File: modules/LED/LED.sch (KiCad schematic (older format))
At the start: 50 parts, among them J1 2, J10 11, J11 12, J12 13, J13 A0, J14 A1, J15 A2, J16 A3, J17 A4, J18 A5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

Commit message: LED rework
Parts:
- removed Q? (x4): IRLML2060, Package_TO_SOT_SMD:SOT-23, symbol Transistor_FET:IRLML2060
- removed R?: 10k, symbol Device:R
- removed U1: 4511, Package_SO:SOIC-16_3.9x9.9mm_P1.27mm, symbol 4xxx_IEEE:4511
- removed U?: 74HC238, symbol 74xx_IEEE:74HC238
- added Q1, Q2, Q3, Q4: IRLML6402, Package_TO_SOT_SMD:SOT-23, symbol Transistor_FET:IRLML6402
- added R14: R, Resistor_SMD:R_0805_2012Metric_Pad1.15x1.40mm_HandSolder, symbol Device:R
- added U1: 74LS247, Package_SO:SOIC-16_3.9x9.9mm_P1.27mm, symbol 74xx:74LS247
- added U2: 74LS139, Package_SO:SOIC-16_3.9x9.9mm_P1.27mm, symbol 74xx_IEEE:74LS139
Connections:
- wire segments 123 -> 107
- no-connect marks 11 -> 17
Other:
- note added: "CA"
- note removed: "CC"
- moved on the sheet: C1, D1, D2, D4, D5, R12

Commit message: Fix LED pcb
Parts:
- removed R14: R, Resistor_SMD:R_0805_2012Metric_Pad1.15x1.40mm_HandSolder, symbol Device:R
- renumbered L1 to HL1
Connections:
- net labels added: D0, D1, D2, D3, Line0
- wire segments 107 -> 108
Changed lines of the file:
@@
 $EndComp
 $Comp
-L CommonLibrary:7seg-4dig-0.4inch L1
+L CommonLibrary:7seg-4dig-0.4inch HL1
 U 1 1 5D7B3B0A
 P 4150 4050
-F 0 "L1" H 4150 4215 50  0000 C CNN
+F 0 "HL1" H 4150 4215 50  0000 C CNN
 F 1 "7seg-4dig-0.4inch" H 4150 4124 50  0000 C CNN
 F 2 "CommonLibrary:7seg-4dig-0.4inch" H 4175 4675 50  0001 C CNN
@@
 U 1 1 5D7C402B
 P 4950 3050
-F 0 "R11" V 4900 2900 50  0000 C CNN
+F 0 "R11" V 4900 2875 50  0000 C CNN
 F 1 "100" V 4950 3050 50  0000 C CNN
 F 2 "Resistor_SMD:R_0805_2012Metric_Pad1.15x1.40mm_HandSolder" V 4880 3050 50  0001 C CNN
@@
 U 1 1 5D7C4561
 P 4950 2900
-F 0 "R10" V 4900 2750 50  0000 C CNN
+F 0 "R10" V 4900 2725 50  0000 C CNN
 F 1 "100" V 4950 2900 50  0000 C CNN
 F 2 "Resistor_SMD:R_0805_2012Metric_Pad1.15x1.40mm_HandSolder" V 4880 2900 50  0001 C CNN
@@
 U 1 1 5D7C4753
 P 4950 2700
-F 0 "R9" V 4900 2550 50  0000 C CNN
+F 0 "R9" V 4900 2525 50  0000 C CNN
 F 1 "100" V 4950 2700 50  0000 C CNN
 F 2 "Resistor_SMD:R_0805_2012Metric_Pad1.15x1.40mm_HandSolder" V 4880 2700 50  0001 C CNN
@@
 U 1 1 5D7C4A05
 P 4950 2550
-F 0 "R8" V 4900 2400 50  0000 C CNN
+F 0 "R8" V 4900 2375 50  0000 C CNN
 F 1 "100" V 4950 2550 50  0000 C CNN
 F 2 "Resistor_SMD:R_0805_2012Metric_Pad1.15x1.40mm_HandSolder" V 4880 2550 50  0001 C CNN
@@
 U 1 1 5D806B1E
 P 5900 1875
-F 0 "R12" V 5825 1925 50  0000 L CNN
+F 0 "R12" V 5800 1825 50  0000 L CNN
 F 1 "10k" V 5900 1825 50  0000 L CNN
 F 2 "Resistor_SMD:R_0805_2012Metric_Pad1.15x1.40mm_HandSolder" V 5830 1875 50  0001 C CNN
@@
 U 1 1 5D82C9F4
 P 1825 4750
-F 0 "R13" H 1895 4796 50  0000 L CNN
-F 1 "10k" H 1895 4705 50  0000 L CNN
+F 0 "R13" V 1725 4675 50  0000 L CNN
+F 1 "10k" V 1825 4675 50  0000 L CNN
 F 2 "Resistor_SMD:R_0805_2012Metric_Pad1.15x1.40mm_HandSolder" V 1755 4750 50  0001 C CNN
 F 3 "~" H 1825 4750 50  0001 C CNN
@@
 U 1 1 5D7D571B
 P 6525 4700
-F 0 "C1" H 6525 4825 50  0000 L CNN
-F 1 "0.1uF" H 6525 4525 50  0000 L CNN
+F 0 "C1" H 6550 4825 50  0000 L CNN
+F 1 "0.1uF" H 6550 4550 50  0000 L CNN
 F 2 "Capacitor_SMD:C_0805_2012Metric_Pad1.15x1.40mm_HandSolder" H 6563 4550 50  0001 C CNN
 F 3 "~" H 6525 4700 50  0001 C CNN
@@
 U 2 1 5D9F2012
 P 3725 2800
-F 0 "U2" H 3725 3416 50  0000 C CNN
-F 1 "74LS139" H 3725 3325 50  0000 C CNN
+F 0 "U2" H 3525 3250 50  0000 C CNN
+F 1 "74LS139" H 3925 3250 50  0000 C CNN
 F 2 "Package_SO:SOIC-16_3.9x9.9mm_P1.27mm" H 3725 2800 50  0001 C CNN
 F 3 "" H 3725 2800 50  0001 C CNN
@@
 	2150 4450 1900 4450
 NoConn ~ 1200 2500
-$Comp
-L Device:R R14
-U 1 1 5DA2086C
-P 2150 5100
-F 0 "R14" H 2220 5146 50  0000 L CNN
-F 1 "R" H 2220 5055 50  0000 L CNN
-F 2 "Resistor_SMD:R_0805_2012Metric_Pad1.15x1.40mm_HandSolder" V 2080 5100 50  0001 C CNN
-F 3 "~" H 2150 5100 50  0001 C CNN
-	1    2150 5100
-	1    0    0    -1
-$EndComp
-$Comp
-L power:GND #PWR02
-U 1 1 5DA20E1A
-P 2150 5250
-F 0 "#PWR02" H 2150 5000 50  0001 C CNN
-F 1 "GND" H 2155 5077 50  0000 C CNN
-F 2 "" H 2150 5250 50  0001 C CNN
-F 3 "" H 2150 5250 50  0001 C CNN
-	1    2150 5250
-	1    0    0    -1
-$EndComp
 $Comp
 L power:GND #PWR06
@@
 NoConn ~ 3450 1775
 NoConn ~ 3450 1925
+Text Label 1425 2800 0    50   ~ 0
+D0
+Text Label 1425 2950 0    50   ~ 0
+D1
+Text Label 1425 3100 0    50   ~ 0
+D2
+Text Label 1425 3250 0    50   ~ 0
+D3
+Text Label 1425 3400 0    50   ~ 0
+Line0
+Wire Wire Line
+	2150 4950 2150 4750
+Connection ~ 2150 4750
 $EndSCHEMATC

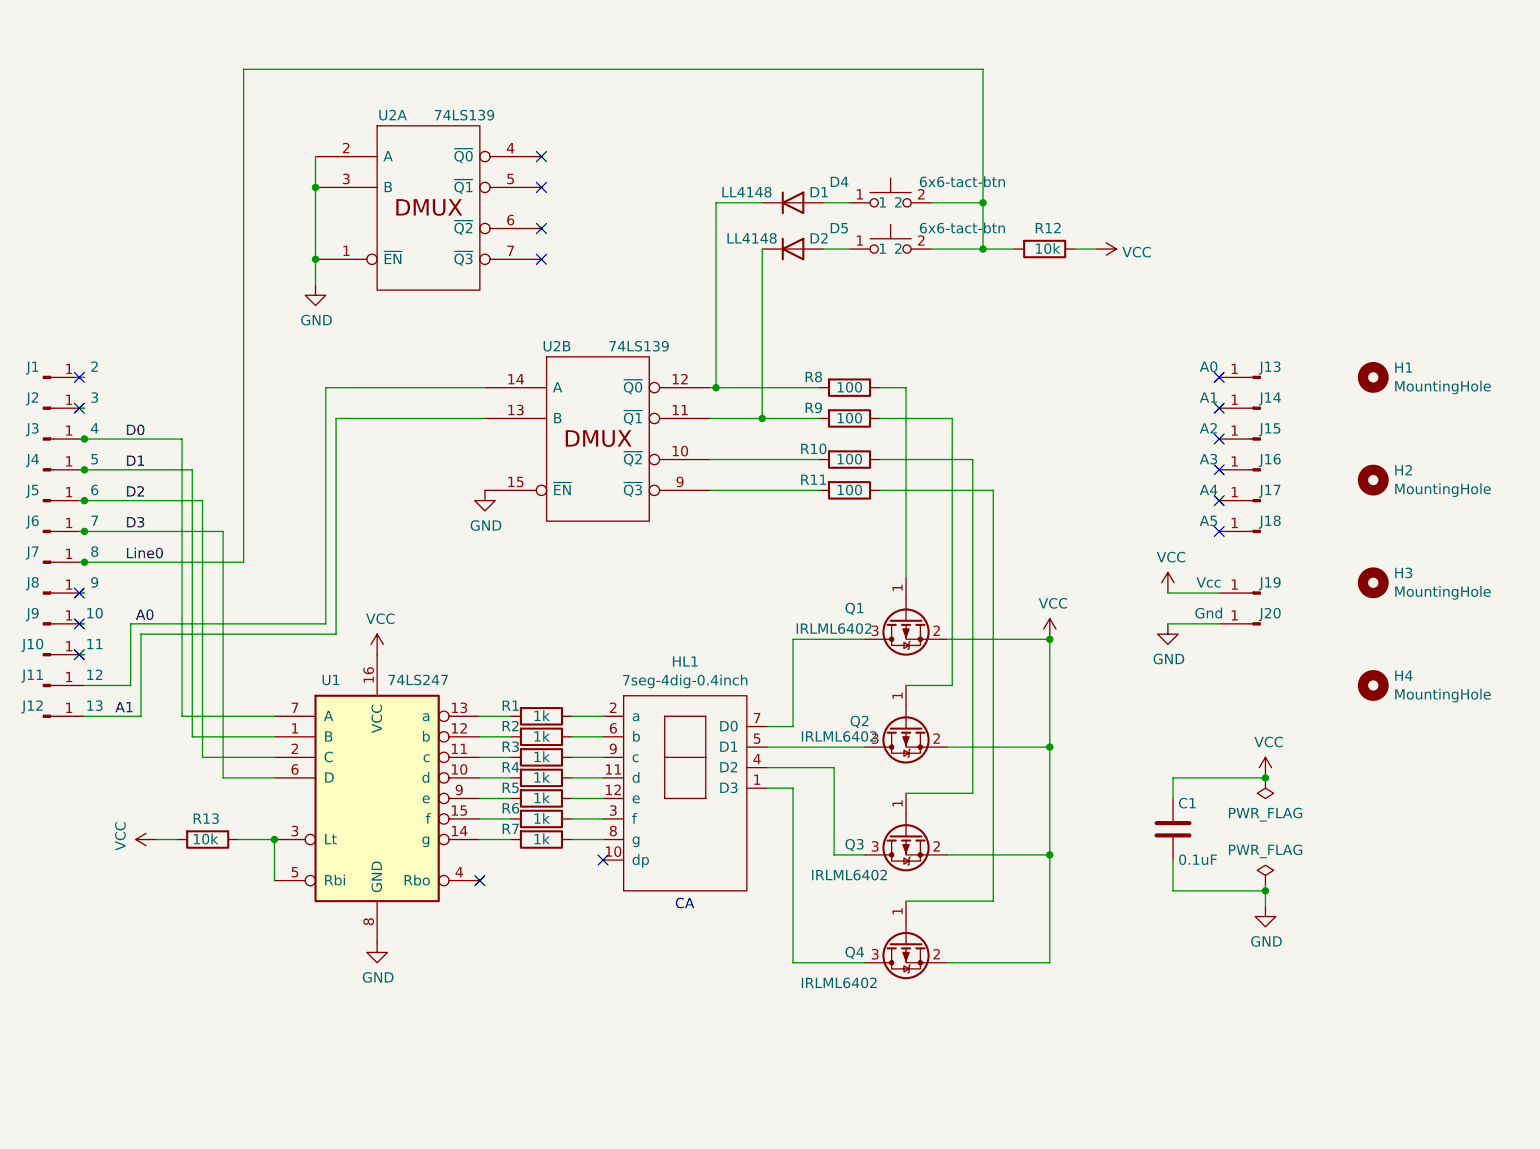
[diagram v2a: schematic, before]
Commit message: LED v2 Pins changed
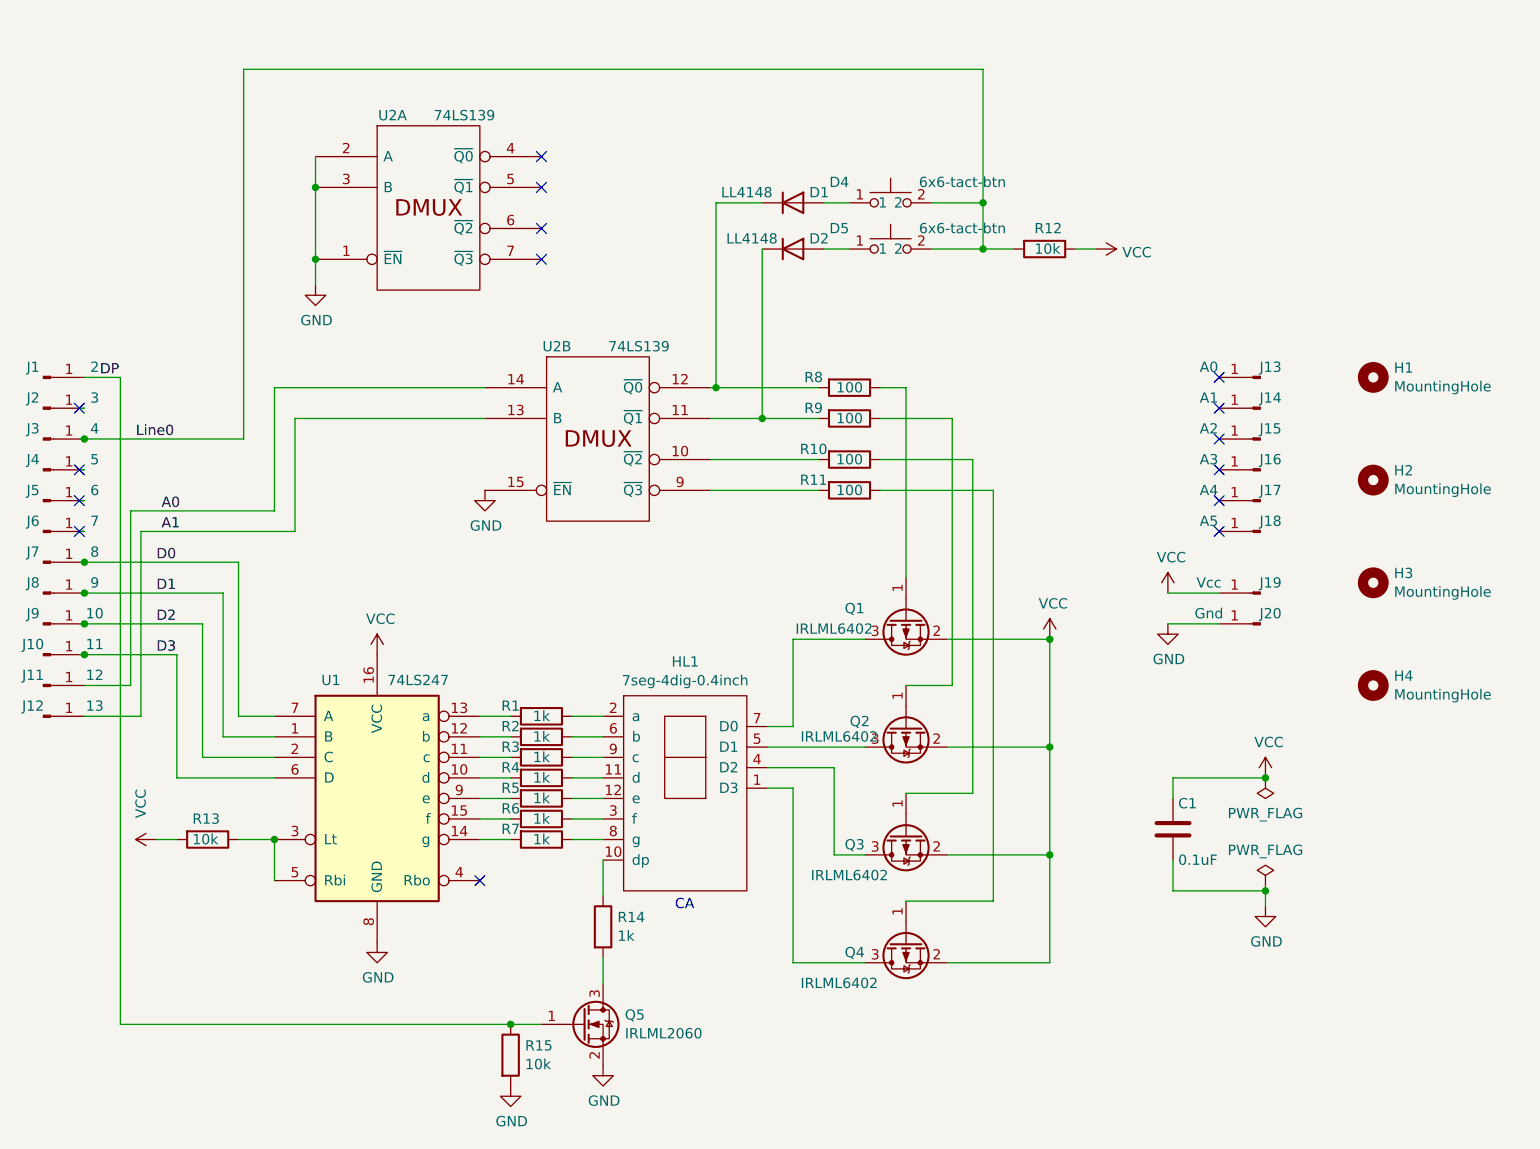
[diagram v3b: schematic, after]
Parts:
- added Q5: IRLML2060, Package_TO_SOT_SMD:SOT-23, symbol Transistor_FET:IRLML2060
- added R14: 1k, Resistor_SMD:R_0805_2012Metric_Pad1.15x1.40mm_HandSolder, symbol Device:R
- added R15: 10k, Resistor_SMD:R_0805_2012Metric_Pad1.15x1.40mm_HandSolder, symbol Device:R
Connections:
- net labels added: DP
- wire segments 108 -> 113
- no-connect marks 17 -> 15
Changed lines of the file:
@@
 P 1575 4750
 F 0 "#PWR0104" H 1575 4600 50  0001 C CNN
-F 1 "VCC" H 1592 4923 50  0000 C CNN
+F 1 "VCC" H 1750 4825 50  0000 C CNN
 F 2 "" H 1575 4750 50  0001 C CNN
 F 3 "" H 1575 4750 50  0001 C CNN
@@
 	1200 2650 1225 2650
 Wire Wire Line
-	1200 2500 1225 2500
-Wire Wire Line
 	1200 2950 1225 2950
 Wire Wire Line
-	1750 2950 1750 4250
-Connection ~ 1225 2950
-Wire Wire Line
-	1225 2950 1750 2950
-Wire Wire Line
 	1200 3100 1225 3100
 Wire Wire Line
-	1800 3100 1800 4350
-Connection ~ 1225 3100
-Wire Wire Line
-	1225 3100 1800 3100
-Wire Wire Line
-	1900 3250 1900 4450
-Wire Wire Line
-	1200 3250 1225 3250
-Connection ~ 1225 3250
-Wire Wire Line
-	1225 3250 1900 3250
-Wire Wire Line
-	1200 2800 1225 2800
-Wire Wire Line
-	1700 2800 1700 4150
-Connection ~ 1225 2800
-Wire Wire Line
-	1225 2800 1700 2800
-Wire Wire Line
-	2000 1000 2000 3400
-Wire Wire Line
-	1200 3400 1225 3400
-Connection ~ 1225 3400
-Wire Wire Line
-	1225 3400 2000 3400
+	2000 1000 2000 2800
 NoConn ~ 1200 2650
 $Comp
@@
 Wire Wire Line
 	1575 4750 1675 4750
-Wire Wire Line
-	1200 3550 1225 3550
-Wire Wire Line
-	1200 3700 1225 3700
-Wire Wire Line
-	1200 3850 1225 3850
 NoConn ~ 6750 3250
 NoConn ~ 6750 2500
@@
 NoConn ~ 6750 2950
 NoConn ~ 6750 3100
-NoConn ~ 3750 4850
 $Comp
 L Mechanical:MountingHole H4
@@
 $EndComp
 Wire Wire Line
-	1450 3700 2400 3700
-Wire Wire Line
-	1450 3700 1450 4000
-Wire Wire Line
-	1500 4150 1500 3750
-Wire Wire Line
-	1500 3750 2450 3750
-Wire Wire Line
 	1225 4150 1500 4150
 Wire Wire Line
 	1225 4000 1450 4000
-NoConn ~ 1200 3700
-NoConn ~ 1200 3850
 $Comp
 L Diode:LL4148 D1
@@
 	1    0    0    -1
 $EndComp
-NoConn ~ 1200 3550
-Text Label 1475 3700 0    50   ~ 0
+Text Label 1600 3150 0    50   ~ 0
 A0
-Text Label 1375 4150 0    50   ~ 0
+Text Label 1600 3250 0    50   ~ 0
 A1
 Text Notes 4100 5100 0    50   ~ 0
@@
 	1975 4750 2150 4750
 Wire Wire Line
-	2150 4150 1700 4150
-Wire Wire Line
-	2150 4250 1750 4250
+	2150 4150 1975 4150
+Wire Wire Line
+	2150 4250 1900 4250
 Wire Wire Line
 	2150 4350 1800 4350
-Wire Wire Line
-	2150 4450 1900 4450
-NoConn ~ 1200 2500
 $Comp
 L power:GND #PWR06
@@
 	1    0    0    -1
 $EndComp
-Wire Wire Line
-	2400 2550 3175 2550
-Wire Wire Line
-	2400 2550 2400 3700
-Wire Wire Line
-	2450 2700 3175 2700
-Wire Wire Line
-	2450 2700 2450 3750
 $Comp
 L Transistor_FET:IRLML6402 Q1
@@
 NoConn ~ 3450 1775
 NoConn ~ 3450 1925
-Text Label 1425 2800 0    50   ~ 0
+Text Label 1575 3400 0    50   ~ 0
 D0
-Text Label 1425 2950 0    50   ~ 0
+Text Label 1575 3550 0    50   ~ 0
 D1
-Text Label 1425 3100 0    50   ~ 0
+Text Label 1575 3700 0    50   ~ 0
 D2
-Text Label 1425 3250 0    50   ~ 0
+Text Label 1575 3850 0    50   ~ 0
 D3
-Text Label 1425 3400 0    50   ~ 0
+Text Label 1475 2800 0    50   ~ 0
 Line0
 Wire Wire Line
 	2150 4950 2150 4750
 Connection ~ 2150 4750
+Wire Wire Line
+	1200 3400 1225 3400
+Connection ~ 1225 3400
+Wire Wire Line
+	1200 3250 1225 3250
+Wire Wire Line
+	1200 3550 1225 3550
+Connection ~ 1225 3550
+Wire Wire Line
+	1200 3700 1225 3700
+Wire Wire Line
+	1800 3700 1800 4350
+Connection ~ 1225 3700
+Wire Wire Line
+	1225 3700 1800 3700
+Wire Wire Line
+	1200 3850 1225 3850
+Connection ~ 1225 3850
+Wire Wire Line
+	1225 3850 1675 3850
+Wire Wire Line
+	1975 3400 1975 4150
+Wire Wire Line
+	1225 3400 1975 3400
+Wire Wire Line
+	1675 3850 1675 4450
+Wire Wire Line
+	1675 4450 2150 4450
+Wire Wire Line
+	1900 3550 1900 4250
+Wire Wire Line
+	1225 3550 1900 3550
+Wire Wire Line
+	1200 2800 1225 2800
+Connection ~ 1225 2800
+Wire Wire Line
+	1225 2800 2000 2800
+Wire Wire Line
+	1500 3250 2250 3250
+Wire Wire Line
+	2250 3250 2250 2700
+Wire Wire Line
+	1500 3250 1500 4150
+Wire Wire Line
+	2250 2700 3175 2700
+Wire Wire Line
+	1450 3150 2150 3150
+Wire Wire Line
+	2150 3150 2150 2550
+Wire Wire Line
+	1450 3150 1450 4000
+Wire Wire Line
+	2150 2550 3175 2550
+NoConn ~ 1200 2950
+NoConn ~ 1200 3100
+NoConn ~ 1200 3250
+$Comp
+L Transistor_FET:IRLML2060 Q5
+U 1 1 5E927114
+P 3650 5650
+F 0 "Q5" H 3856 5696 50  0000 L CNN
+F 1 "IRLML2060" H 3856 5605 50  0000 L CNN
+F 2 "Package_TO_SOT_SMD:SOT-23" H 3850 5575 50  0001 L CIN
+F 3 "https://www.infineon.com/dgdl/irlml2060pbf.pdf?fileId=5546d462533600a401535664b7fb25ee" H 3650 5650 50  0001 L CNN
+	1    3650 5650
+	1    0    0    -1
+$EndComp
+$Comp
+L power:GND #PWR0105
+U 1 1 5E92954A
+P 3750 5850
+F 0 "#PWR0105" H 3750 5600 50  0001 C CNN
+F 1 "GND" H 3755 5677 50  0000 C CNN
+F 2 "" H 3750 5850 50  0001 C CNN
+F 3 "" H 3750 5850 50  0001 C CNN
+	1    3750 5850
+	1    0    0    -1
+$EndComp
+$Comp
+L Device:R R14
+U 1 1 5E92A2EF
+P 3750 5175
+F 0 "R14" H 3820 5221 50  0000 L CNN
+F 1 "1k" H 3820 5130 50  0000 L CNN
+F 2 "Resistor_SMD:R_0805_2012Metric_Pad1.15x1.40mm_HandSolder" V 3680 5175 50  0001 C CNN
+F 3 "~" H 3750 5175 50  0001 C CNN
+	1    3750 5175
+	1    0    0    -1
+$EndComp
+Wire Wire Line
+	3750 4850 3750 5025
+Wire Wire Line
+	3750 5325 3750 5450
+Wire Wire Line
+	1225 2500 1400 2500
+Wire Wire Line
+	1400 2500 1400 5650
+Wire Wire Line
+	1400 5650 3300 5650
+$Comp
+L Device:R R15
+U 1 1 5E938856
+P 3300 5800
+F 0 "R15" H 3370 5846 50  0000 L CNN
+F 1 "10k" H 3370 5755 50  0000 L CNN
+F 2 "Resistor_SMD:R_0805_2012Metric_Pad1.15x1.40mm_HandSolder" V 3230 5800 50  0001 C CNN
+F 3 "~" H 3300 5800 50  0001 C CNN
+	1    3300 5800
+	1    0    0    -1
+$EndComp
+Connection ~ 3300 5650
+Wire Wire Line
+	3300 5650 3450 5650
+$Comp
+L power:GND #PWR0106
+U 1 1 5E939925
+P 3300 5950
+F 0 "#PWR0106" H 3300 5700 50  0001 C CNN
+F 1 "GND" H 3305 5777 50  0000 C CNN
+F 2 "" H 3300 5950 50  0001 C CNN
+F 3 "" H 3300 5950 50  0001 C CNN
+	1    3300 5950
+	1    0    0    -1
+$EndComp
+Text Label 1300 2500 0    50   ~ 0
+DP
 $EndSCHEMATC

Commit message: Add resistor
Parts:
- added R16: 100, Resistor_SMD:R_0805_2012Metric_Pad1.15x1.40mm_HandSolder, symbol Device:R
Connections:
- wire segments 113 -> 114
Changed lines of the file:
@@
 Text Notes 4100 5100 0    50   ~ 0
 CA
-Wire Wire Line
-	2000 1000 5600 1000
 $Comp
 L 74xx_IEEE:74LS139 U2
@@
 Text Label 1300 2500 0    50   ~ 0
 DP
+$Comp
+L Device:R R16
+U 1 1 5E8E75A2
+P 3850 1000
+F 0 "R16" V 3643 1000 50  0000 C CNN
+F 1 "100" V 3734 1000 50  0000 C CNN
+F 2 "Resistor_SMD:R_0805_2012Metric_Pad1.15x1.40mm_HandSolder" V 3780 1000 50  0001 C CNN
+F 3 "~" H 3850 1000 50  0001 C CNN
+	1    3850 1000
+	0    1    1    0
+$EndComp
+Wire Wire Line
+	2000 1000 3700 1000
+Wire Wire Line
+	4000 1000 5600 1000
 $EndSCHEMATC

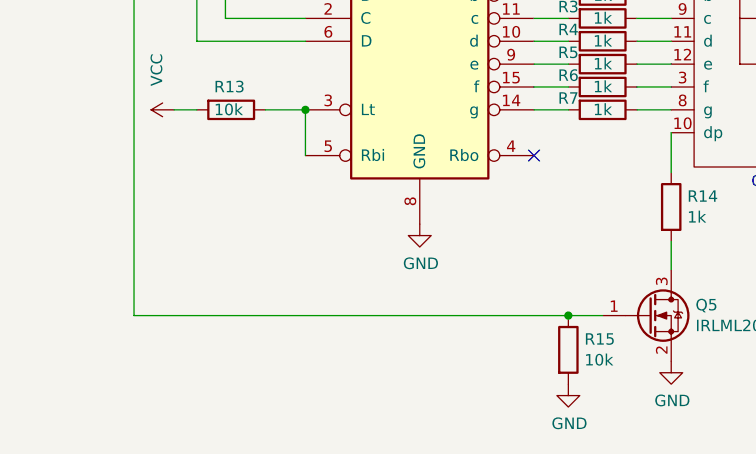
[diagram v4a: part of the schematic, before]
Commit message: Add jumper for decimal point. Small fixes.
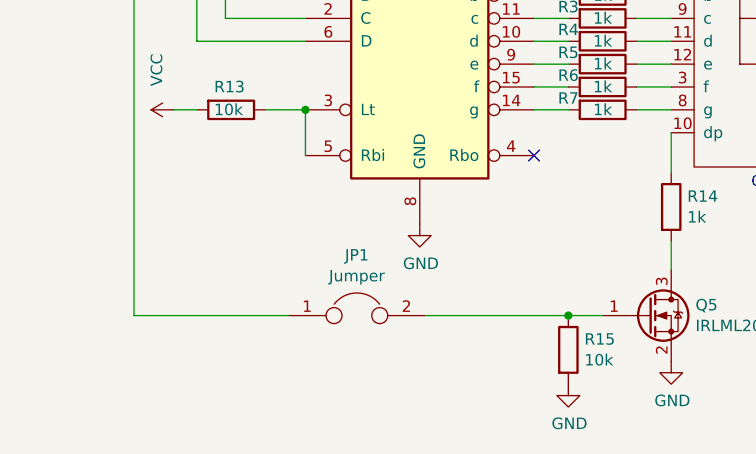
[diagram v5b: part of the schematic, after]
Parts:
- added JP1: Jumper, Connector_PinHeader_2.54mm:PinHeader_1x02_P2.54mm_Vertical, symbol Device:Jumper
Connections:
- wire segments 114 -> 115
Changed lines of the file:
@@
 Wire Wire Line
 	1400 2500 1400 5650
-Wire Wire Line
-	1400 5650 3300 5650
 $Comp
 L Device:R R15
@@
 	1    0    0    -1
 $EndComp
-Connection ~ 3300 5650
 Wire Wire Line
 	3300 5650 3450 5650
@@
 Wire Wire Line
 	4000 1000 5600 1000
+$Comp
+L Device:Jumper JP1
+U 1 1 5E952979
+P 2375 5650
+F 0 "JP1" H 2375 5914 50  0000 C CNN
+F 1 "Jumper" H 2375 5823 50  0000 C CNN
+F 2 "Connector_PinHeader_2.54mm:PinHeader_1x02_P2.54mm_Vertical" H 2375 5650 50  0001 C CNN
+F 3 "~" H 2375 5650 50  0001 C CNN
+	1    2375 5650
+	1    0    0    -1
+$EndComp
+Wire Wire Line
+	1400 5650 2075 5650
+Wire Wire Line
+	2675 5650 3300 5650
+Connection ~ 3300 5650
 $EndSCHEMATC
